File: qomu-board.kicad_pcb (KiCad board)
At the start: 6 copper layers, 28.1 x 10.6 mm, 68 parts, among them IC1 EOS-S3, J1 FTSH-105-01-L-DV-K, J2 825437-4, J3 MC-HVT1-S02-G, Q1 RV1C002UN, Q2 RV1C002UN, Q3 RV1C002UN, SW2 Captouch Pads, U1 MIC5504-3.3YMT, U10 UHD1110-FKA, U2 MIC5504-3.3YMT, U4 GD25Q16C, U5 MC3635, U9 USB-B

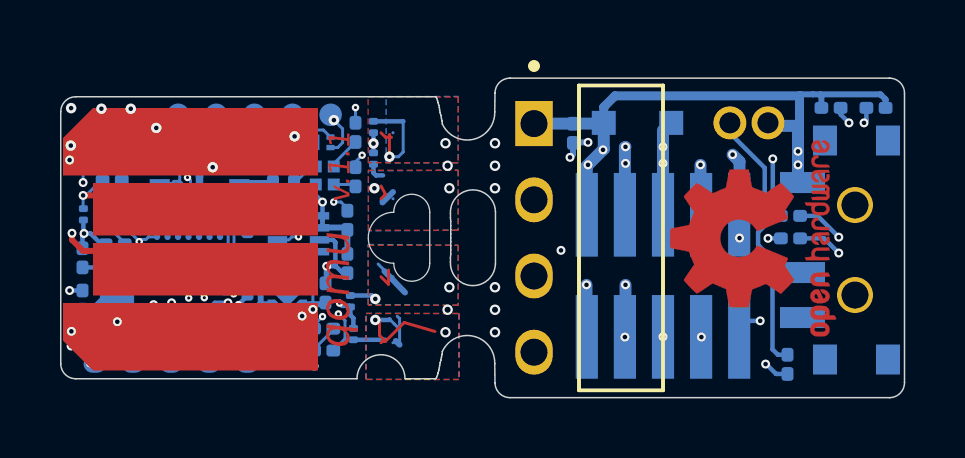
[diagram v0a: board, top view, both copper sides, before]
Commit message: Added bulk capacitors to EOS internal VDD1/1. Removed C11
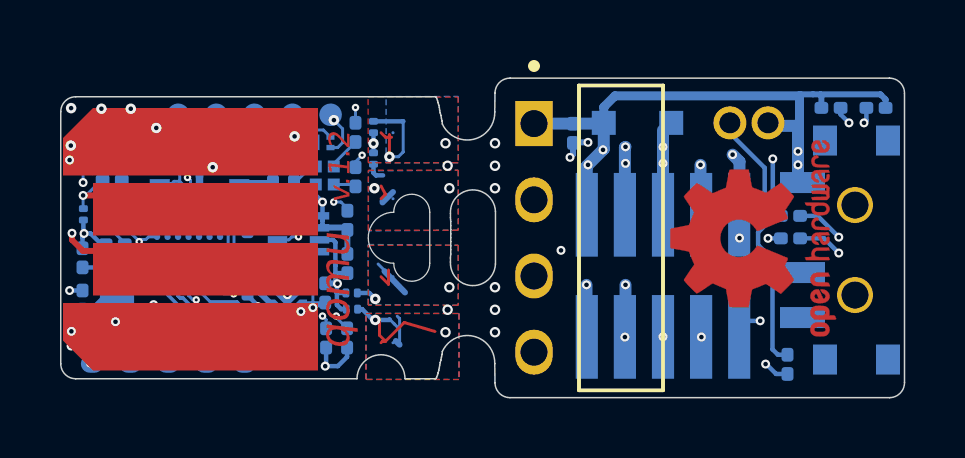
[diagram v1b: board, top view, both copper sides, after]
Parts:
- removed C11: 100n, qomu-board-footprints:C_0201_0603Metric
- added C15: 2u2/10V, qomu-board-footprints:C_0201_0603Metric, B.Cu at (22.4, 24.9)
- added C16: 2u2/10V, qomu-board-footprints:C_0201_0603Metric, B.Cu at (21.7, 24.9)
- U4: value GD25Q16C -> GD25Q16CEIGR; footprint qomu-board-footprints:GD25Q16CEIGR -> qomu-board:GD25Q16CEIGR
- moved TP10 3.36 mm to (18.1, 25.9)
- moved C7 1.95 mm to (24.8, 24.8)
- moved C6 1.67 mm to (23.1, 24.9), turned to 270 degrees
- moved R3 0.89 mm to (26.6, 25.1), turned to 270 degrees
- moved R2 0.87 mm to (23.8, 25.1), turned to 270 degrees
- moved D4 0.83 mm to (26.7, 24.2), turned to 180 degrees
- moved N3 0.75 mm to (20.9, 21.7)
- moved C9 0.62 mm to (21.0, 24.9), turned to 270 degrees
- moved R5 0.46 mm to (24.8, 25.5)
- moved R4 0.32 mm to (25.9, 25.1), turned to 270 degrees
- moved D2 0.28 mm to (26.7, 23.6), turned to 180 degrees
- moved TP1 0.09 mm to (18.1, 25.9)
- moved TP2 0.09 mm to (23.1, 25.9)
- moved TP3 0.09 mm to (20.6, 25.9)
- moved TP9 0.09 mm to (21.9, 25.9)
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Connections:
- C7 pad 1: /VCCIOB -> GND
- C7 pad 2: GND -> /VCCIOB
- IC1 pad A2: Net-(IC1-PadA2) -> /VDD1
- IC1 pad A3: Net-(IC1-PadA3) -> /VDD2
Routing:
- net /VDD2: track 0.00 -> 2.14 mm
- net /VDD1: track 0.00 -> 1.61 mm
- net /LED_G: track 13.3 -> 12.4 mm
- net /TOUCH_1: track 14.4 -> 13.5 mm
- net /I2C_SDA: track 8.33 -> 7.46 mm
- net /VCCIOB: track 6.05 -> 5.24 mm
- net Net-(IC1-PadA5): track 2.14 -> 2.88 mm, vias 2 -> 0
- net /SWD_IO: track 31.9 -> 31.2 mm
- net /E1: track 12.5 -> 12.0 mm
- net GND: track 51.3 -> 50.8 mm, vias 57 -> 55
- net +3V3: track 58.5 -> 58.0 mm, vias 28 -> 30
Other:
- board text added: "rev.1.2"
- board text added: "v.1.2"
- board text removed: "rev.1.1"
- board text removed: "v.1.1"

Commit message: Updated revision markings
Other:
- board text added: "rev.1.1"
- board text added: "v.1.1"
- board text removed: "rev.1.2"
- board text removed: "v.1.2"
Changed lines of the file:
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@@
   )
   (layers
-    (0 Top signal hide)
-    (1 In1.Cu signal hide)
+    (0 Top signal)
+    (1 In1.Cu signal)
     (2 In2.Cu signal)
     (3 In3.Cu signal)
@@
   )
   (setup
-    (last_trace_width 0.2)
+    (last_trace_width 0.1)
     (user_trace_width 0.1)
     (user_trace_width 0.15)
@@
     (effects (font (size 0.5 0.5) (thickness 0.12)) (justify mirror))
   )
-  (gr_text rev.1.2 (at 24.7 19.33) (layer In1.Cu)
+  (gr_text rev.1.1 (at 24.7 19.33) (layer In1.Cu)
     (effects (font (size 0.8 0.7) (thickness 0.15) italic))
   )
@@
   (gr_poly (pts (xy 29.707585 23.27) (xy 30.05 23.12) (xy 30.05 20.52) (xy 29.7 20.32) (xy 29.7 19.57) (xy 27.3075 19.57) (xy 27.3 24.02) (xy 28.5075 24.02) (xy 29.715 24.02)) (layer F.Mask) (width 0.1))
   (gr_poly (pts (xy 29.707585 23.27) (xy 30.05 23.12) (xy 30.05 20.52) (xy 29.7 20.32) (xy 29.7 19.57) (xy 27.3075 19.57) (xy 27.3 24.02) (xy 28.5075 24.02) (xy 29.715 24.02)) (layer B.Mask) (width 0.1))
-  (gr_text v.1.2 (at 26.325 19.445 90) (layer Top)
+  (gr_text v.1.1 (at 26.325 19.445 90) (layer Top)
     (effects (font (size 0.7 0.7) (thickness 0.15) italic))
   )
@@
   (via (at 31.5 18.65) (size 0.35) (drill 0.2) (layers Top Bottom) (net 0))
   (via (at 31.5 19.4) (size 0.35) (drill 0.2) (layers Top Bottom) (net 0))
-  (via blind (at 23.08 24.27) (size 0.3) (drill 0.15) (layers In3.Cu In4.Cu) (net 2))
-  (via blind (at 23.39 24.56) (size 0.3) (drill 0.15) (layers In2.Cu In3.Cu) (net 2))
   (via blind (at 25.14 25.63) (size 0.3) (drill 0.15) (layers In3.Cu In4.Cu) (net 1))
   (via (at 34 19.12) (size 0.3) (drill 0.15) (layers Top Bottom) (net 1))
@@
   (segment (start 25.14 25.63) (end 25.14 26.01) (width 0.2) (layer In4.Cu) (net 1))
   (segment (start 25.14 26.01) (end 25.14 24.79) (width 0.2) (layer Bottom) (net 1))
+  (via blind (at 23.08 24.27) (size 0.3) (drill 0.15) (layers In3.Cu In4.Cu) (net 2))
+  (via blind (at 23.39 24.56) (size 0.3) (drill 0.15) (layers In2.Cu In3.Cu) (net 2))
   (via (at 41.6 18.92) (size 0.3) (drill 0.15) (layers Top Bottom) (net 2))
   (via (at 41.6 19.37) (size 0.3) (drill 0.15) (layers Top Bottom) (net 2))

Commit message: LED_G reconnected to FBIO9
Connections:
- IC1 pad A5: Net-(IC1-PadA5) -> /LED_G
- IC1 pad A6: /LED_G -> Net-(IC1-PadA6)
- R2 pad 1: Net-(IC1-PadA5) -> /LED_G
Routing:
- net /LED_G: track 12.4 -> 16.6 mm
- net Net-(IC1-PadA5): track 2.88 -> 0.00 mm
